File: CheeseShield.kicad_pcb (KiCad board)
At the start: 2 copper layers, 90.5 x 53.3 mm, 27 parts, among them J1 MS3 Toggle, J2 MS2 Toggle, J3 MS1 Toggle, J4 Power Screw Terminal, J5 JST XH_Stepper, J6 Temp2 3PinFan, J7 TempBed 3PinFan, J8 Temp1 3PinFan, J9 SSR Connection, M1 LM2596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

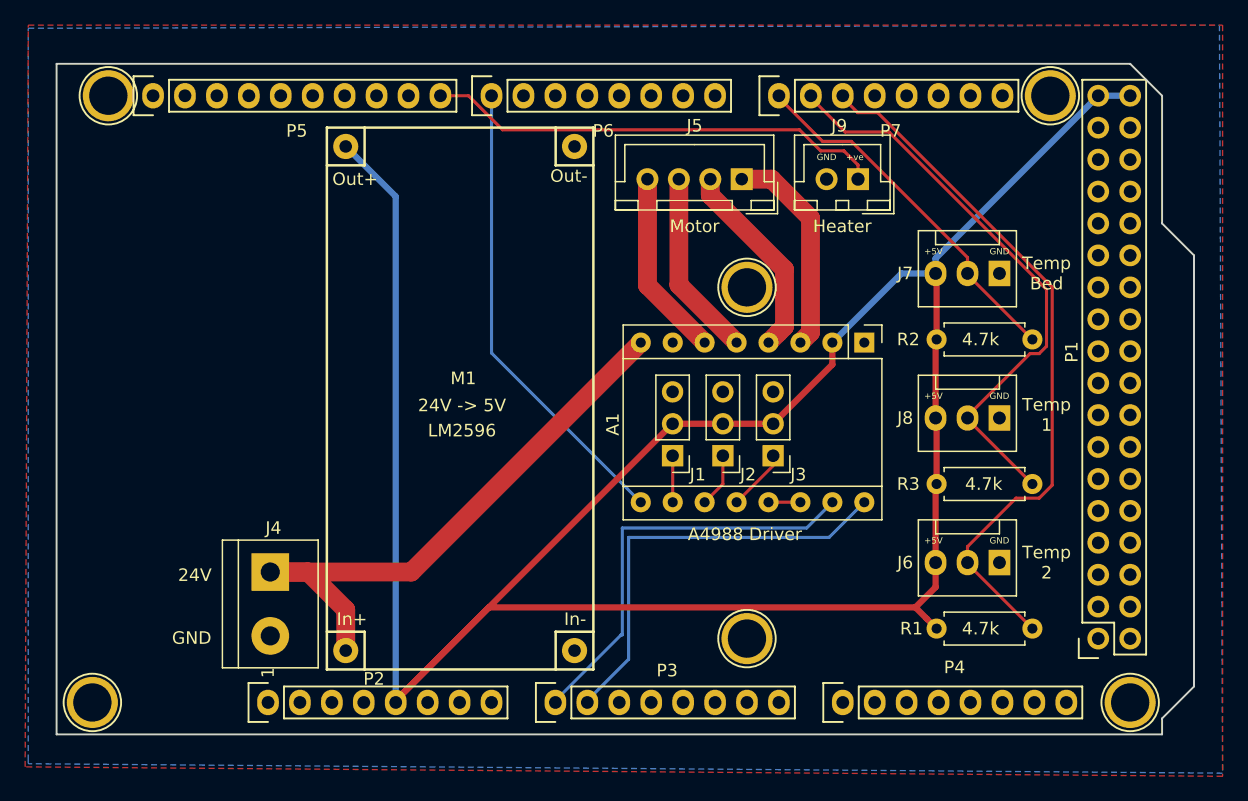
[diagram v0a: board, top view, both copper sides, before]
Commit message: feat: Added in bluetooth and servo headers
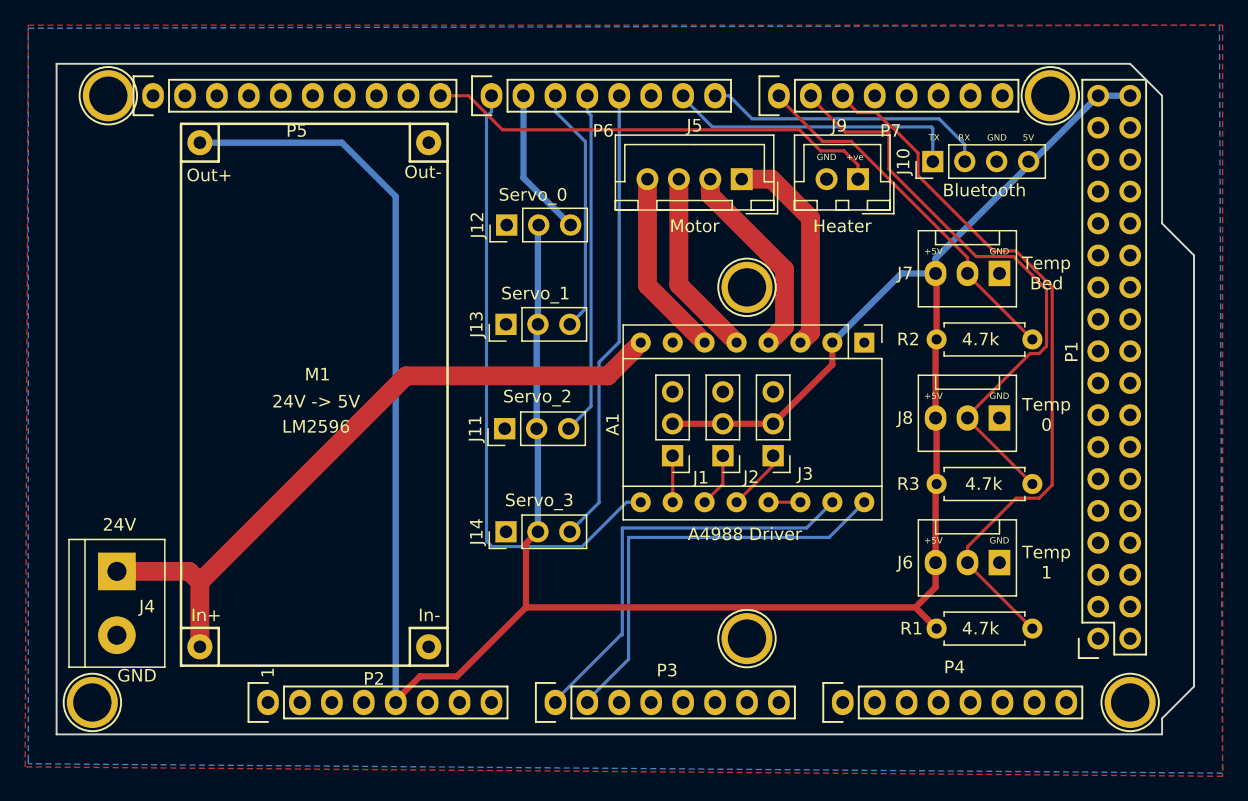
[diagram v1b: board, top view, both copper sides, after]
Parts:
- added J10: BlueTooth Connection, Pin_Headers:Pin_Header_Straight_1x04_Pitch2.54mm, F.Cu at (184.2, 76.1)
- added J11: Servo_2 Header, Pin_Headers:Pin_Header_Straight_1x03_Pitch2.54mm, F.Cu at (150.2, 97.3)
- added J12: Servo_0 Header, Pin_Headers:Pin_Header_Straight_1x03_Pitch2.54mm, F.Cu at (150.3, 81.2)
- added J13: Servo_1 Header, Pin_Headers:Pin_Header_Straight_1x03_Pitch2.54mm, F.Cu at (150.2, 89.0)
- added J14: Servo_3 Header, Pin_Headers:Pin_Header_Straight_1x03_Pitch2.54mm, F.Cu at (150.2, 105.5)
- J6: value Temp2 3PinFan -> Temp1 3PinFan
- J8: value Temp1 3PinFan -> Temp0 3PinFan
- moved J4 12.2 mm to (119.3, 108.7)
- moved M1 11.6 mm to (124.4, 116.2)
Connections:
- J6 pad 2: TEMP_2 -> TEMP_1
- J8 pad 2: TEMP_1 -> TEMP_0
- P6 pad 2: /6(**) -> SERVO_0
- P6 pad 3: /5(**) -> SERVO_1
- P6 pad 4: /4(**) -> SERVO_2
- P6 pad 5: /3(**) -> SERVO_3
- P6 pad 7: /1(Tx0) -> TX
- P6 pad 8: /0(Rx0) -> RX
- P7 pad 2: TEMP_1 -> TEMP_0
- P7 pad 3: TEMP_2 -> TEMP_1
- R1 pad 2: TEMP_2 -> TEMP_1
- R3 pad 2: TEMP_1 -> TEMP_0
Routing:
- net TEMP_2: track 56.2 -> 0.00 mm
- net TEMP_0: track 0.00 -> 47.6 mm
- net SERVO_3: track 0.00 -> 36.3 mm
- net SERVO_2: track 0.00 -> 27.3 mm
- net TX: track 0.00 -> 23.7 mm
- net RX: track 0.00 -> 22.8 mm
- net SERVO_1: track 0.00 -> 19.7 mm
- net EN: track 37.3 -> 49.5 mm
- net SERVO_0: track 0.00 -> 11.8 mm
- net +5V: track 200.4 -> 212.1 mm
- net TEMP_1: track 45.9 -> 57.3 mm
- net +24V: track 47.5 -> 55.1 mm
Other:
- board text added: "5V"
- board text added: "Bluetooth"
- board text added: "RX"
- board text added: "Servo_0"
- board text added: "Servo_1"
- board text added: "Servo_2"
- board text added: "Servo_3"
- board text added: "TX"
- board text added: "Temp 0"
- board text removed: "Temp 2"
